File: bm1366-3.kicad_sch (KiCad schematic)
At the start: 82 parts, among them U14 BM1366_mode1, U25 ADP171AUJ-R7, U26 ADP171AUJ-R7, U28 TLV3544

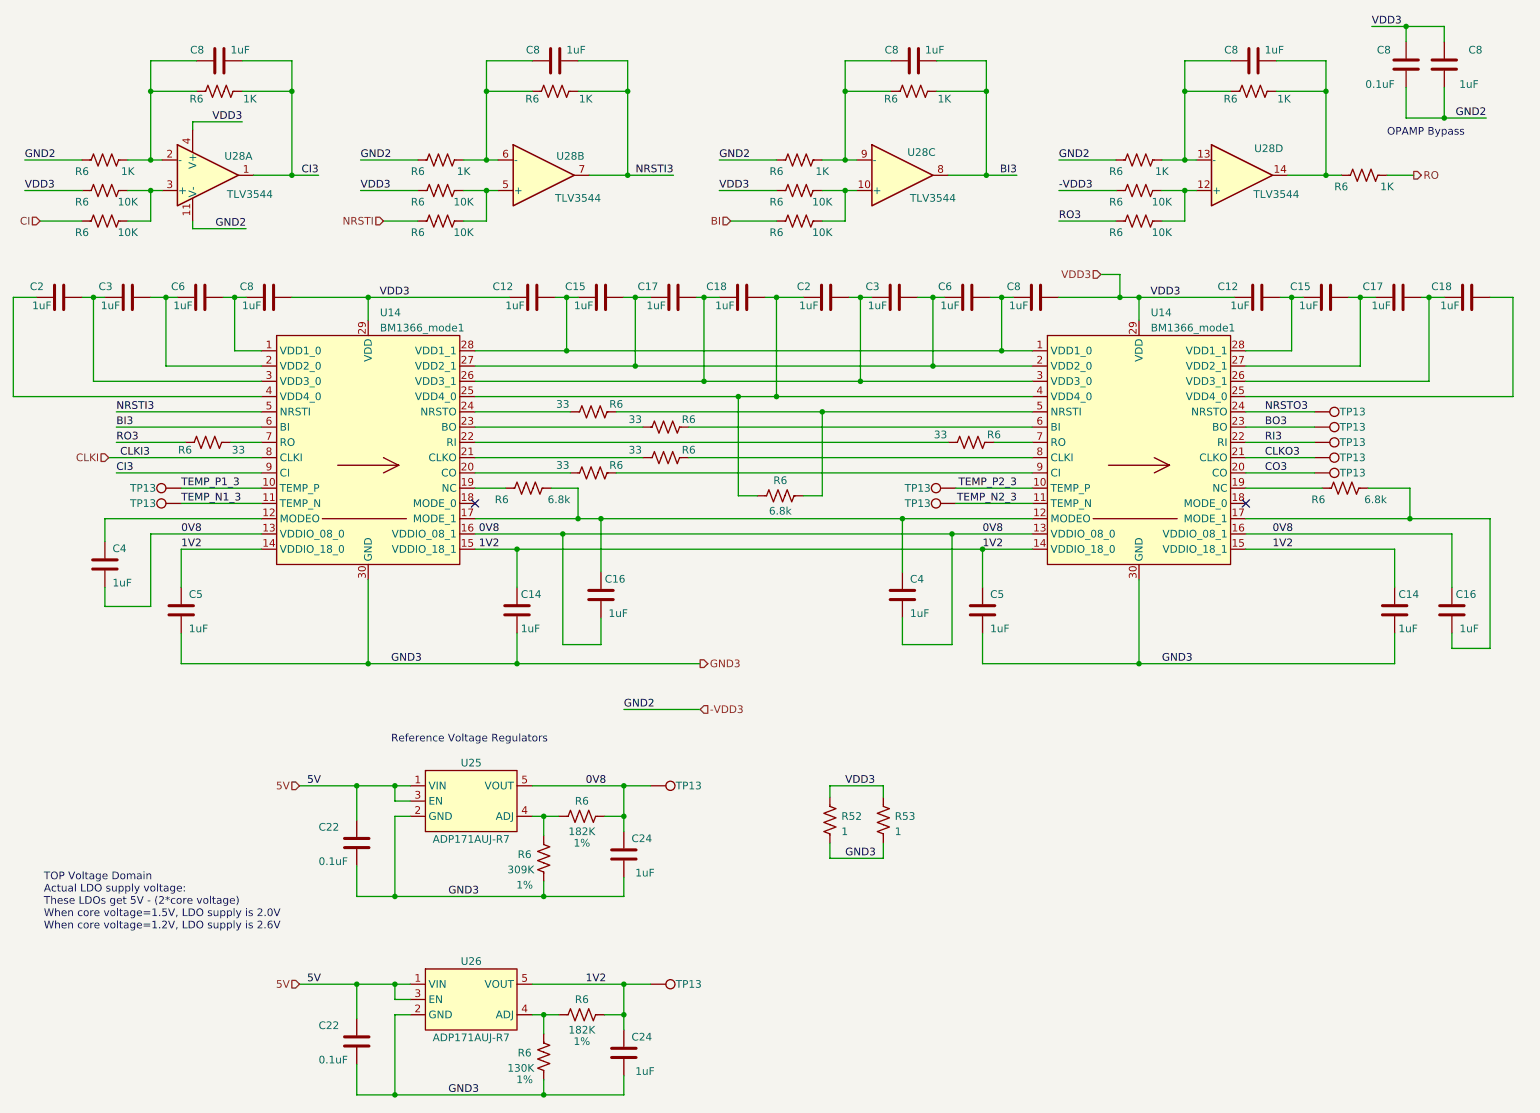
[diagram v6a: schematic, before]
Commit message: add oscillators, large bypass caps, start routing reference voltages
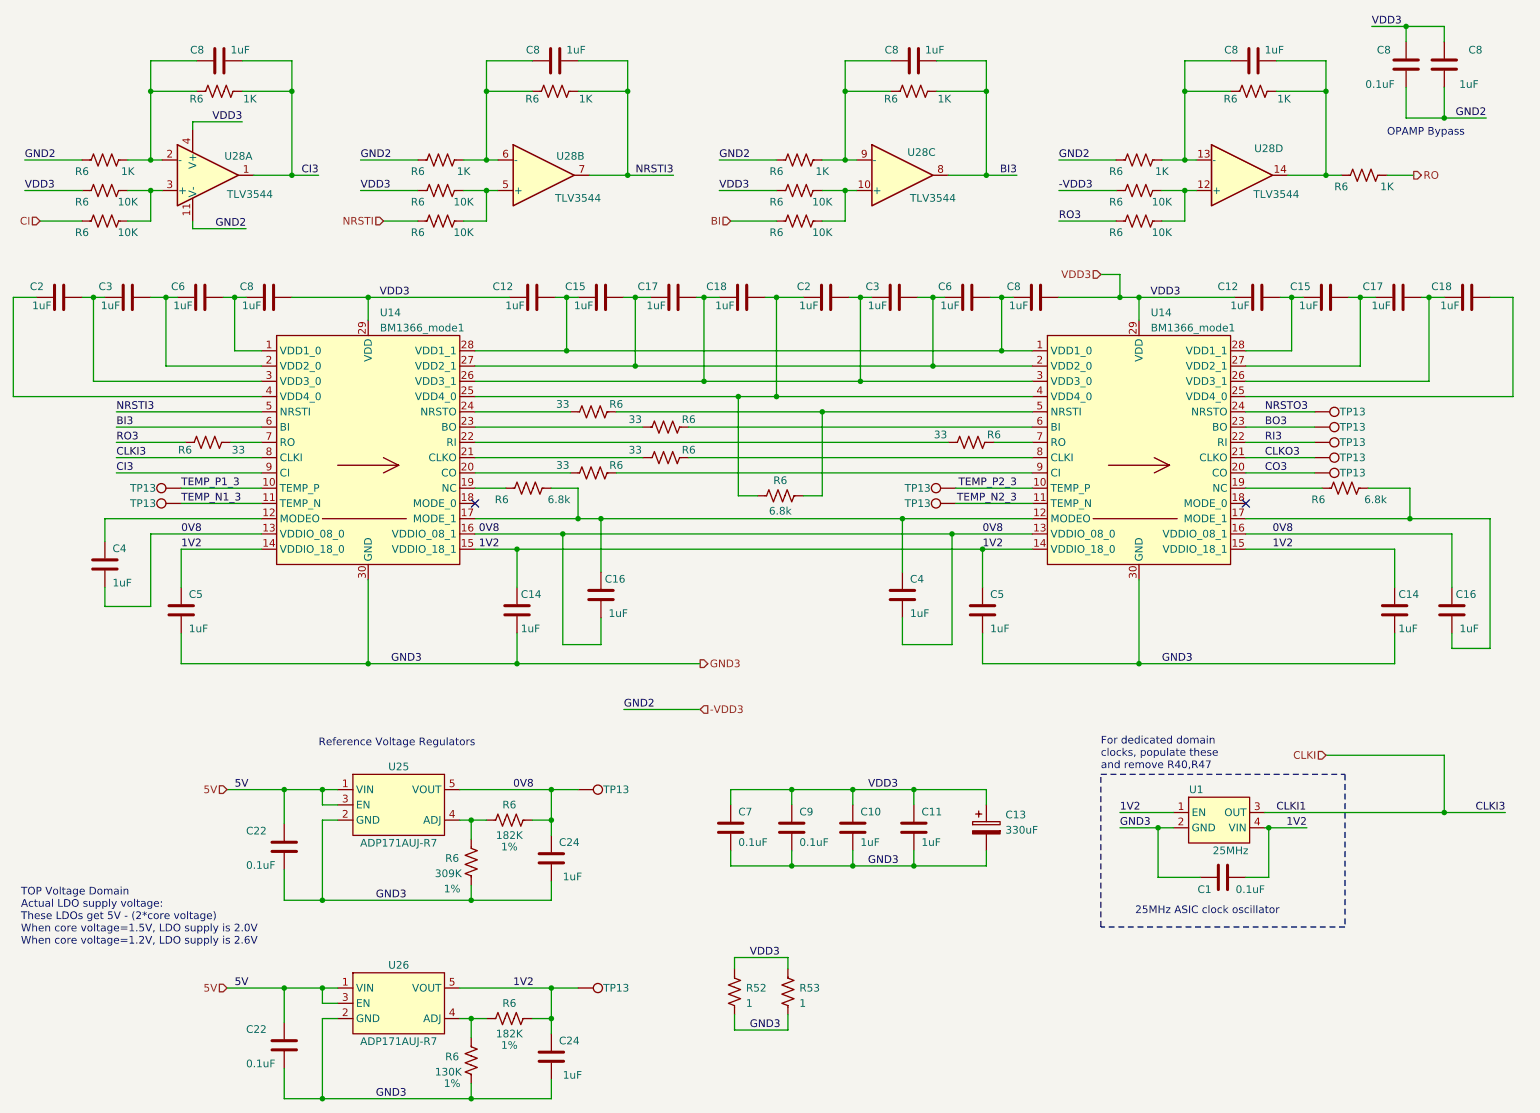
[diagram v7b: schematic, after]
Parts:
- added C1, C7, C9: 0.1uF, Capacitor_SMD:C_0402_1005Metric, symbol Device:C
- added C10, C11: 1uF, Capacitor_SMD:C_0402_1005Metric, symbol Device:C
- added C13: 330uF, Capacitor_Tantalum_SMD:CP_EIA-7343-31_Kemet-D_Pad2.25x2.55mm_HandSolder, symbol Device:C_Polarized
- added U1: 25MHz, bitaxe:O 25,0-JO32-B-1V3-1-T1-LF, symbol bitaxe:oscillator
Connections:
- net 1V2: now also C1.2, U1.1 (EN), U1.4 (VIN)
- net CLKI: now also U1.3 (OUT)
- net GND3: now also C1.1, C10.2, C11.2, C13.2, C7.2, C9.2, U1.2 (GND)
- net VDD3: now also C10.1, C11.1, C13.1, C7.1, C9.1
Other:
- note added: "25MHz ASIC clock oscillator"
- note added: "For dedicated domain clocks, populate these and remove R40,R47"
- moved on the sheet: C22, C24, R52, R53, R6, TP13, U25, U26

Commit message: added some DK part numbers
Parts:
- C8: DK 587-5514-1-ND -> 1292-1639-1-ND; PARTNO EMK105BJ105MV-F -> 0402X104K100CT
- U25, U26: DK (none) -> 505-ADP171AUJZ-R7CT-ND; PARTNO (none) -> ADP171AUJZ-R7
- U28: DK (none) -> 296-45352-1-ND; PARTNO (none) -> TLV3544IPWR
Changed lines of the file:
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@@
       (effects (font (size 1.27 1.27)) hide)
     )
-    (property "DK" "587-5514-1-ND" (at 246.38 24.13 0)
-      (effects (font (size 1.27 1.27)) hide)
-    )
-    (property "PARTNO" "EMK105BJ105MV-F" (at 246.38 24.13 0)
+    (property "DK" "1292-1639-1-ND" (at 246.38 24.13 0)
+      (effects (font (size 1.27 1.27)) hide)
+    )
+    (property "PARTNO" "0402X104K100CT" (at 246.38 24.13 0)
       (effects (font (size 1.27 1.27)) hide)
     )
@@
     )
     (property "Datasheet" "https://www.digikey.com/en/products/detail/analog-devices-inc/ADP171AUJZ-R7/2000964" (at 78.74 138.43 0)
+      (effects (font (size 1.27 1.27)) hide)
+    )
+    (property "DK" "505-ADP171AUJZ-R7CT-ND" (at 78.74 146.05 0)
+      (effects (font (size 1.27 1.27)) hide)
+    )
+    (property "PARTNO" "ADP171AUJZ-R7" (at 78.74 146.05 0)
       (effects (font (size 1.27 1.27)) hide)
     )
@@
     )
     (property "Datasheet" "https://www.digikey.com/en/products/detail/analog-devices-inc/ADP171AUJZ-R7/2000964" (at 78.74 171.45 0)
+      (effects (font (size 1.27 1.27)) hide)
+    )
+    (property "DK" "505-ADP171AUJZ-R7CT-ND" (at 78.74 179.07 0)
+      (effects (font (size 1.27 1.27)) hide)
+    )
+    (property "PARTNO" "ADP171AUJZ-R7" (at 78.74 179.07 0)
       (effects (font (size 1.27 1.27)) hide)
     )
@@
     )
     (property "Datasheet" "https://www.ti.com/lit/ds/symlink/tlv3542.pdf" (at 101.6 42.545 0)
+      (effects (font (size 1.27 1.27)) hide)
+    )
+    (property "DK" "296-45352-1-ND" (at 100.33 42.545 0)
+      (effects (font (size 1.27 1.27)) hide)
+    )
+    (property "PARTNO" "TLV3544IPWR" (at 100.33 42.545 0)
       (effects (font (size 1.27 1.27)) hide)
     )
@@
       (effects (font (size 1.27 1.27)) hide)
     )
+    (property "DK" "296-45352-1-ND" (at 160.02 42.545 0)
+      (effects (font (size 1.27 1.27)) hide)
+    )
+    (property "PARTNO" "TLV3544IPWR" (at 160.02 42.545 0)
+      (effects (font (size 1.27 1.27)) hide)
+    )
     (pin "1")
     (pin "11")
@@
       (effects (font (size 1.27 1.27)) hide)
     )
+    (property "DK" "296-45352-1-ND" (at 216.535 42.545 0)
+      (effects (font (size 1.27 1.27)) hide)
+    )
+    (property "PARTNO" "TLV3544IPWR" (at 216.535 42.545 0)
+      (effects (font (size 1.27 1.27)) hide)
+    )
     (pin "1")
     (pin "11")
@@
       (effects (font (size 1.27 1.27)) hide)
     )
+    (property "DK" "296-45352-1-ND" (at 44.45 42.545 0)
+      (effects (font (size 1.27 1.27)) hide)
+    )
+    (property "PARTNO" "TLV3544IPWR" (at 44.45 42.545 0)
+      (effects (font (size 1.27 1.27)) hide)
+    )
